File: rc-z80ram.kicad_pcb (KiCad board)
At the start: 2 copper layers, 99.1 x 49.9 mm, 19 parts, among them J1 Conn_01x39_Male, J2 Conn_01x10_Male, U1 Z80CPU, U2 AS6C1008, U3 DS1233-5, U4 4017, X1 7.3728MHz

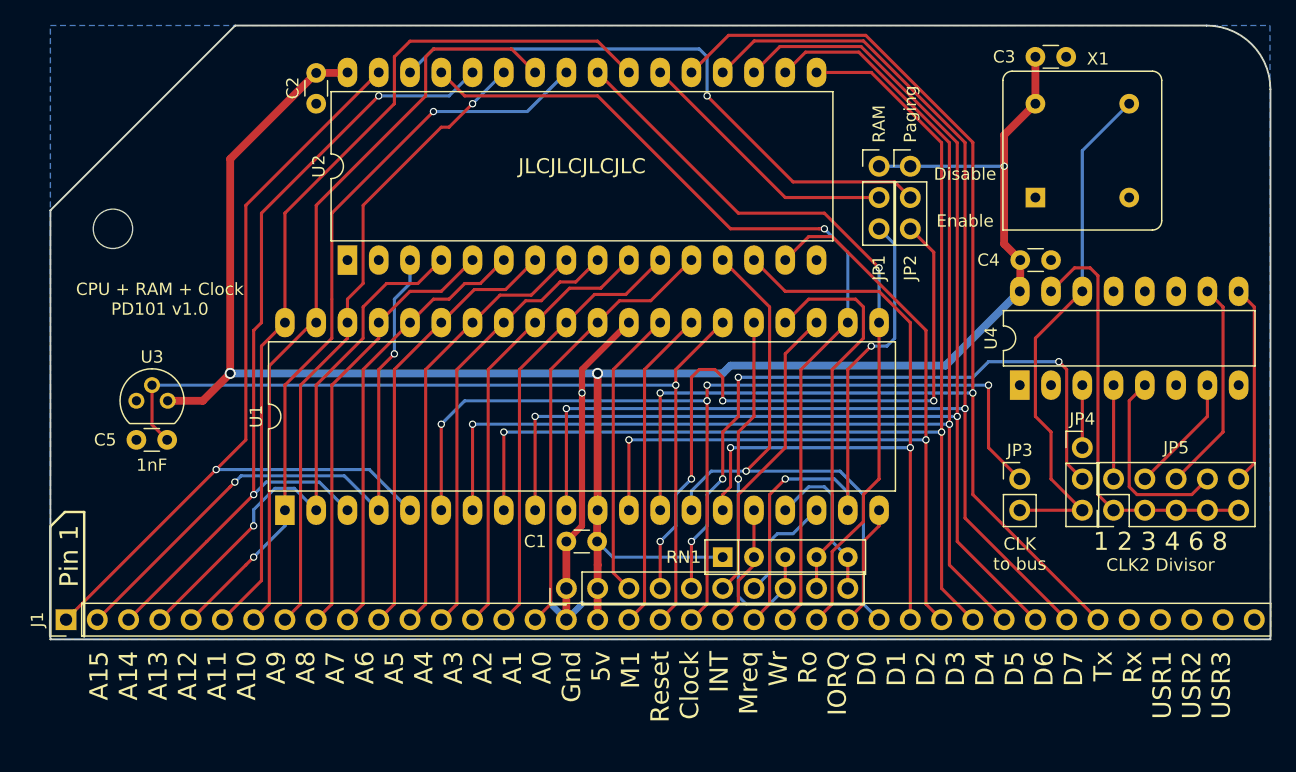
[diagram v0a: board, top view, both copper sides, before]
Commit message: Move components, clean up routing
Move components in order to shorten and neaten clock traces. Make jumpers easier to reach, move oscillator to bottom of card to reduce shorting risk.
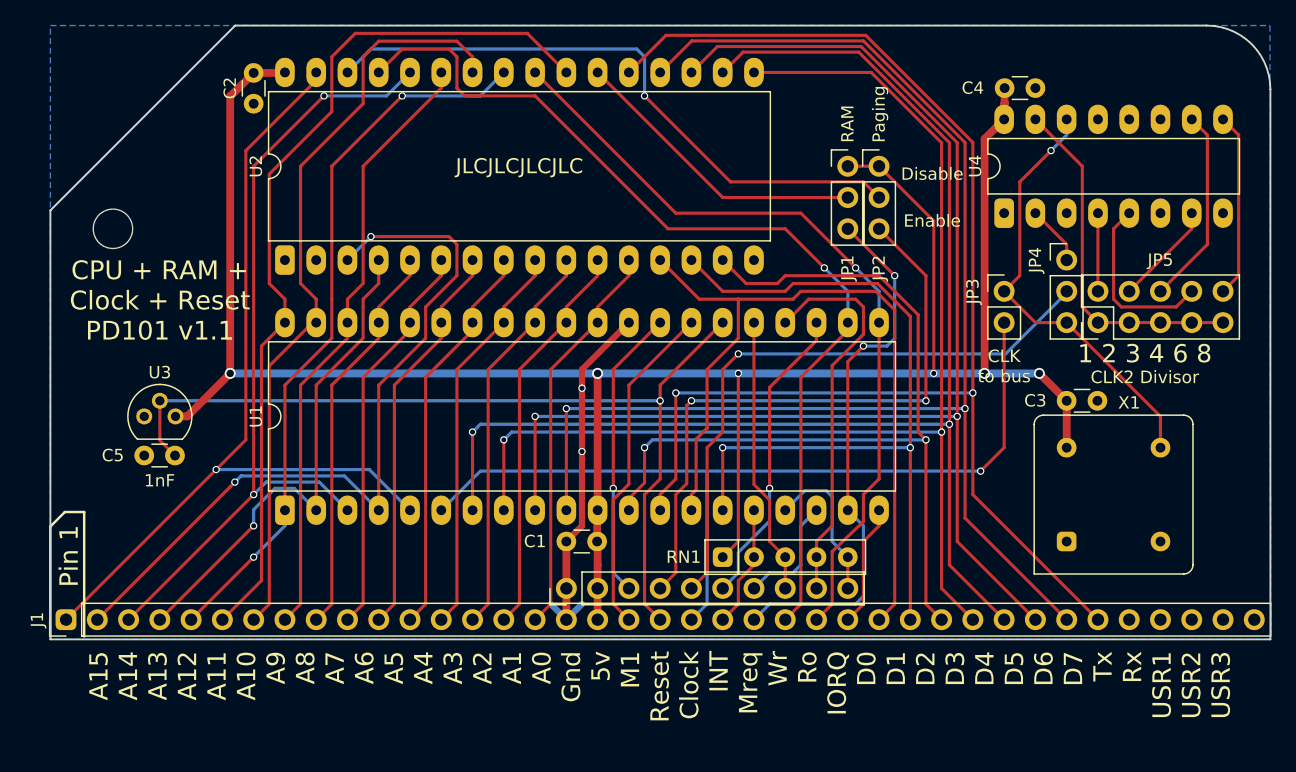
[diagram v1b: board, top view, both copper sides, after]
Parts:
- J1: value Conn_01x39_Male -> RC2014
- J2: value Conn_01x10_Male -> RC2014_Enh
- moved C3 28.1 mm to (234.9, 132.1)
- moved X1 28.1 mm to (234.9, 143.5)
- moved JP3 15.3 mm to (229.9, 123.2)
- moved JP5 15.3 mm to (237.5, 125.7)
- moved JP4 15.3 mm to (234.9, 120.7)
- moved C4 14.0 mm to (232.4, 106.7)
- moved U4 14.0 mm to (229.9, 116.8)
- moved C2 5.08 mm to (168.9, 108.0)
- moved U2 5.08 mm to (171.4, 120.7)
- moved JP1 2.54 mm to (217.2, 113.0)
- moved JP2 2.54 mm to (219.7, 113.0)
- moved C5 1.42 mm to (160.0, 136.5)
- moved U3 1.42 mm to (160.0, 133.3)
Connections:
- JP3 pad 1: CLK -> OSC
- JP3 pad 2: OSC -> CLK
- U4 pad 2: Net-(U4-Pad2) -> /CDIV
- U4 pad 3: /CDIV -> Net-(U4-Pad3)
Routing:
- net +5V: track 164.3 -> 186.8 mm, vias 3 -> 6
- net D0: track 47.2 -> 65.7 mm, vias 1 -> 0
- net A14: track 50.2 -> 63.0 mm
- net CLK: track 80.5 -> 70.6 mm, vias 4 -> 1
- net OSC: track 42.8 -> 35.5 mm, vias 0 -> 1
- net ~BUSRQ: track 29.9 -> 22.6 mm, vias 1 -> 0
- net ~WR: track 71.7 -> 77.9 mm
- net D1: track 58.9 -> 65.2 mm
- net CLK2: track 55.6 -> 49.5 mm, vias 4 -> 1
- net /DRESET: track 34.6 -> 28.8 mm
- net D5: track 103.9 -> 109.0 mm
- net D6: track 107.0 -> 112.1 mm
- net D4: track 103.4 -> 108.1 mm
- net D3: track 94.2 -> 98.9 mm
- net D7: track 105.6 -> 109.9 mm
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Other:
- board text added: "CPU + RAM + Clock + Reset PD101 v1.1"
- board text added: "Clock 7.3728 MHz 3.6864 MHz 2.4576 MHz 1.8432 MHz 1.2288 MHz 0.9216 MHz"
- board text added: "Divisor /1 /2 /3 /4 /6 /8"
- board text removed: "CPU + RAM + Clock PD101 v1.0"
- board text removed: "Clock 7.3278 MHz 3.6864 MHz 2.4576 MHz 1.8432 MHz 1.2288 MHz 0.9216 MHz"
- board text removed: "Ratio 1 2 3 4 6 8"

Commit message: Added silkscreen decorations
Added silkscreen decorations to resemble the general shape of RC2014 cards.
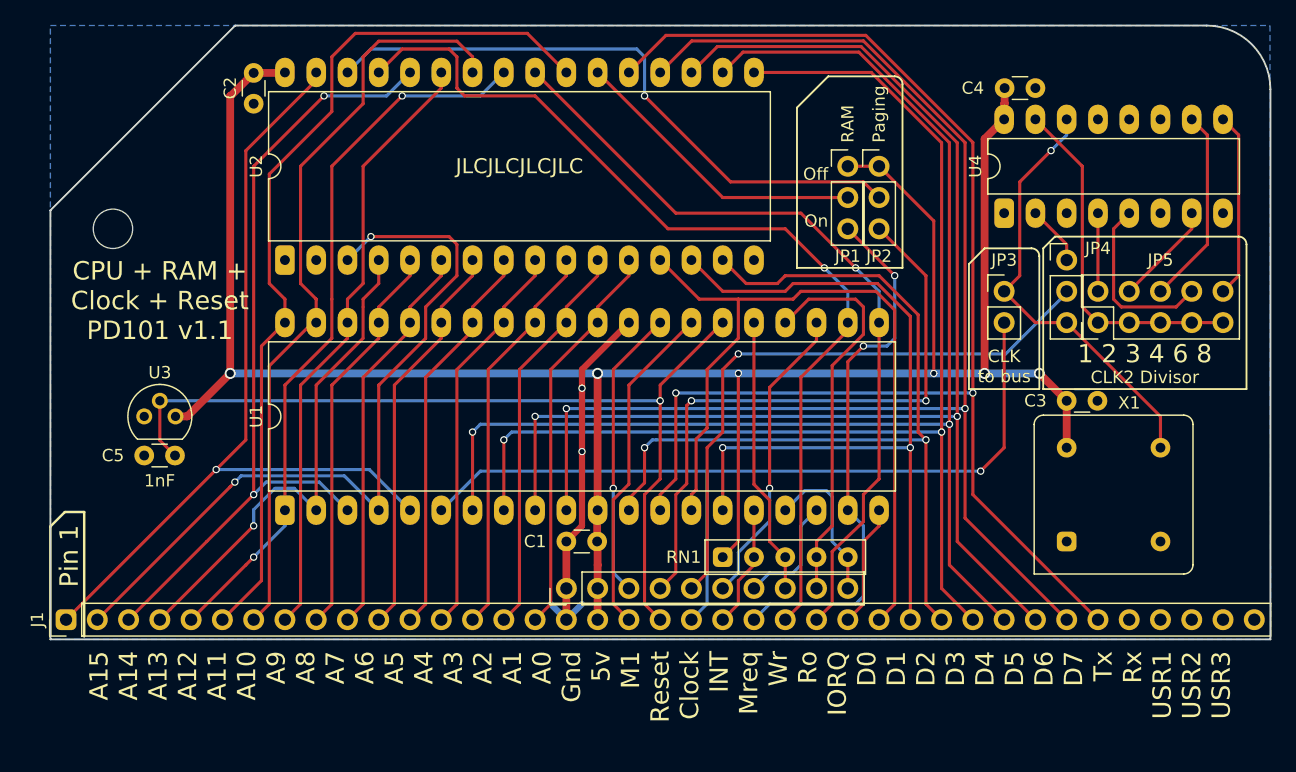
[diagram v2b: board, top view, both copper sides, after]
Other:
- board text added: "Off"
- board text added: "On"
- board text removed: "Disable"
- board text removed: "Enable"
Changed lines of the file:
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@@
   (general
     (thickness 1.6)
-    (drawings 159)
+    (drawings 178)
     (tracks 476)
     (zones 0)
@@
   )
   (setup
-    (last_trace_width 0.254)
+    (last_trace_width 0.25)
     (user_trace_width 0.254)
     (user_trace_width 0.508)
@@
     (descr "Through hole straight pin header, 1x03, 2.54mm pitch, single row")
     (tags "Through hole pin header THT 1x03 2.54mm single row")
-    (fp_text reference JP4 (at -2.54 0 90) (layer F.SilkS)
+    (fp_text reference JP4 (at 2.54 -0.9525 180) (layer F.SilkS)
       (effects (font (size 1 1) (thickness 0.15)))
     )
@@
     (descr "Through hole straight pin header, 1x02, 2.54mm pitch, single row")
     (tags "Through hole pin header THT 1x02 2.54mm single row")
-    (fp_text reference JP3 (at -2.54 0 90) (layer F.SilkS)
+    (fp_text reference JP3 (at 0 -2.54 180) (layer F.SilkS)
       (effects (font (size 1 1) (thickness 0.15)))
     )
@@
     (descr "Through hole straight pin header, 1x03, 2.54mm pitch, single row")
     (tags "Through hole pin header THT 1x03 2.54mm single row")
-    (fp_text reference JP2 (at 0 8.255 270) (layer F.SilkS)
+    (fp_text reference JP2 (at 0 7.3025) (layer F.SilkS)
       (effects (font (size 1 1) (thickness 0.15)))
     )
@@
     (descr "Through hole straight pin header, 1x03, 2.54mm pitch, single row")
     (tags "Through hole pin header THT 1x03 2.54mm single row")
-    (fp_text reference JP1 (at 0 8.255 90) (layer F.SilkS)
+    (fp_text reference JP1 (at 0 7.3025 180) (layer F.SilkS)
       (effects (font (size 1 1) (thickness 0.15)))
     )
@@
     (pad "" np_thru_hole circle (at 0 0) (size 3.2 3.2) (drill 3.2) (layers *.Cu *.Mask F.SilkS))
   )
+  (gr_text "CPU + RAM +\nClock + Reset\nPD101 v1.1" (at 219.71 107.315) (layer B.SilkS)
+    (effects (font (size 1.5 1.5) (thickness 0.3)) (justify mirror))
+  )
+  (gr_arc (start 220.98 106.3625) (end 221.615 106.3625) (angle -90) (layer F.SilkS) (width 0.15))
+  (gr_line (start 215.5825 105.7275) (end 220.98 105.7275) (layer F.SilkS) (width 0.15))
+  (gr_line (start 213.0425 108.2675) (end 215.5825 105.7275) (layer F.SilkS) (width 0.15))
+  (gr_line (start 213.0425 121.285) (end 213.0425 108.2675) (layer F.SilkS) (width 0.15))
+  (gr_line (start 221.615 121.285) (end 213.0425 121.285) (layer F.SilkS) (width 0.15))
+  (gr_line (start 221.615 106.3625) (end 221.615 121.285) (layer F.SilkS) (width 0.15))
+  (gr_arc (start 248.92 119.38) (end 249.555 119.38) (angle -90) (layer F.SilkS) (width 0.15))
+  (gr_line (start 249.555 131.1275) (end 233.045 131.1275) (layer F.SilkS) (width 0.15))
+  (gr_line (start 249.555 119.38) (end 249.555 131.1275) (layer F.SilkS) (width 0.15))
+  (gr_line (start 233.9975 118.745) (end 248.92 118.745) (layer F.SilkS) (width 0.15))
+  (gr_line (start 233.045 119.6975) (end 233.9975 118.745) (layer F.SilkS) (width 0.15))
+  (gr_line (start 233.045 131.1275) (end 233.045 119.6975) (layer F.SilkS) (width 0.15))
+  (gr_arc (start 232.0925 120.3325) (end 232.7275 120.3325) (angle -90) (layer F.SilkS) (width 0.15))
+  (gr_line (start 228.2825 119.6975) (end 232.0925 119.6975) (layer F.SilkS) (width 0.15))
+  (gr_line (start 227.0125 120.9675) (end 228.2825 119.6975) (layer F.SilkS) (width 0.15))
+  (gr_line (start 227.0125 131.1275) (end 227.0125 120.9675) (layer F.SilkS) (width 0.15))
+  (gr_line (start 232.7275 131.1275) (end 227.0125 131.1275) (layer F.SilkS) (width 0.15))
+  (gr_line (start 232.7275 120.3325) (end 232.7275 131.1275) (layer F.SilkS) (width 0.15))
   (gr_text "CLK\nto bus" (at 229.87 129.286) (layer F.SilkS)
     (effects (font (size 1.016 1.016) (thickness 0.15)))
@@
     (effects (font (size 1 1) (thickness 0.15)) (justify left))
   )
-  (gr_text Enable (at 224.028 117.475) (layer F.SilkS)
-    (effects (font (size 1 1) (thickness 0.15)))
-  )
-  (gr_text Disable (at 224.028 113.665) (layer F.SilkS)
-    (effects (font (size 1 1) (thickness 0.15)))
+  (gr_text On (at 215.5825 117.475) (layer F.SilkS)
+    (effects (font (size 1 1) (thickness 0.15)) (justify right))
+  )
+  (gr_text Off (at 215.5825 113.665) (layer F.SilkS)
+    (effects (font (size 1 1) (thickness 0.15)) (justify right))
   )
   (gr_text "CLK2 Divisor" (at 241.3 130.175) (layer F.SilkS)
@@
   )
   (gr_text "CPU + RAM +\nClock + Reset\nPD101 v1.1" (at 161.29 123.952) (layer F.SilkS)
-    (effects (font (size 1.524 1.524) (thickness 0.2032)))
+    (effects (font (size 1.5 1.5) (thickness 0.3)))
   )
   (gr_line (start 167.4114 101.6) (end 152.4 116.6114) (angle 90) (layer Edge.Cuts) (width 0.15))

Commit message: Add BOM, tidy up schematic
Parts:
- U1: value Z80CPU -> Z84C0008
- U4: value 4017 -> CD74HC4017
